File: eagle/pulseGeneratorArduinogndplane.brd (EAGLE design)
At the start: 100 x 80 mm, 64 parts, among them U1 ARDUINOR3-DIMENSION, U2 AD9954YSVZ, U3 LT1962EMS8-1.8PBF, U4 LT1962EMS8-1.8PBF, U7 TXB0108PWR

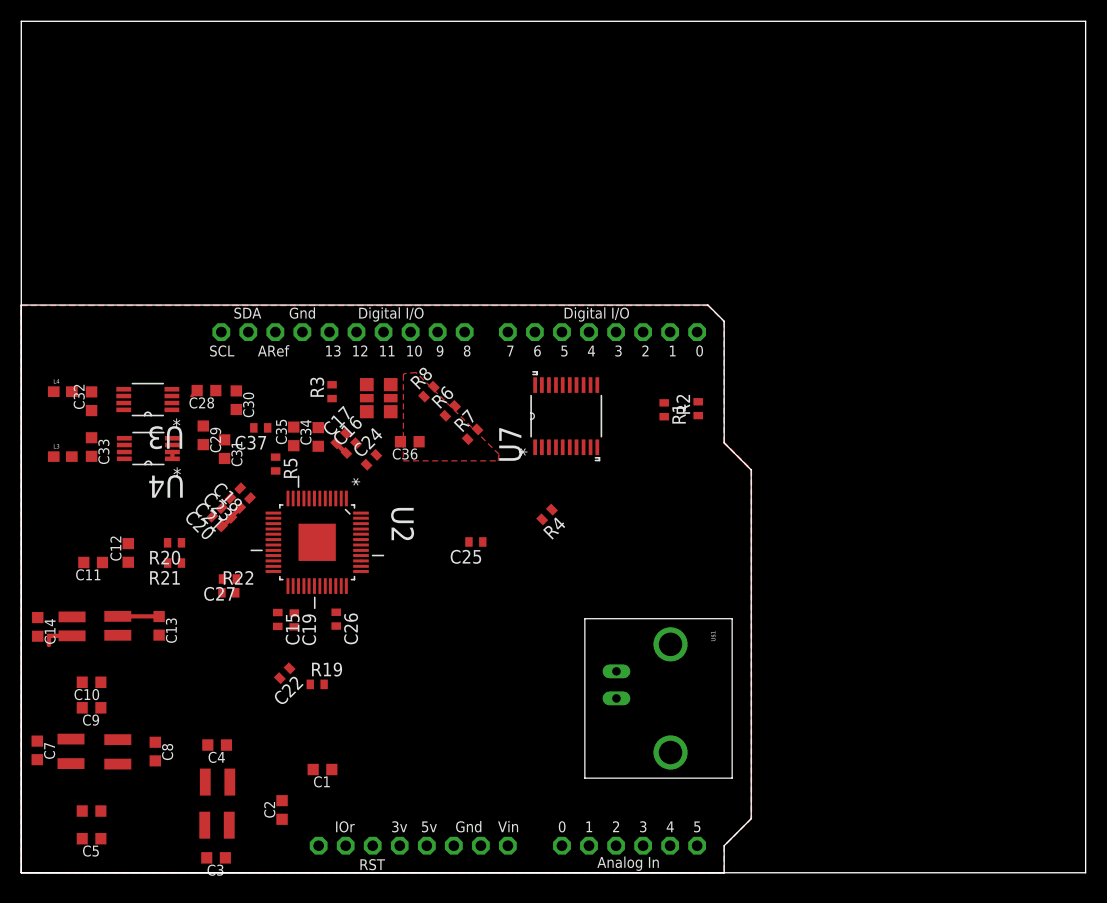
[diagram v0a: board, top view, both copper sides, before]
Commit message: Revert "Deleted all routes to try and fix."
This reverts commit 5f491c1068aea24b9851c2c5770cd8edc15ed6a6.
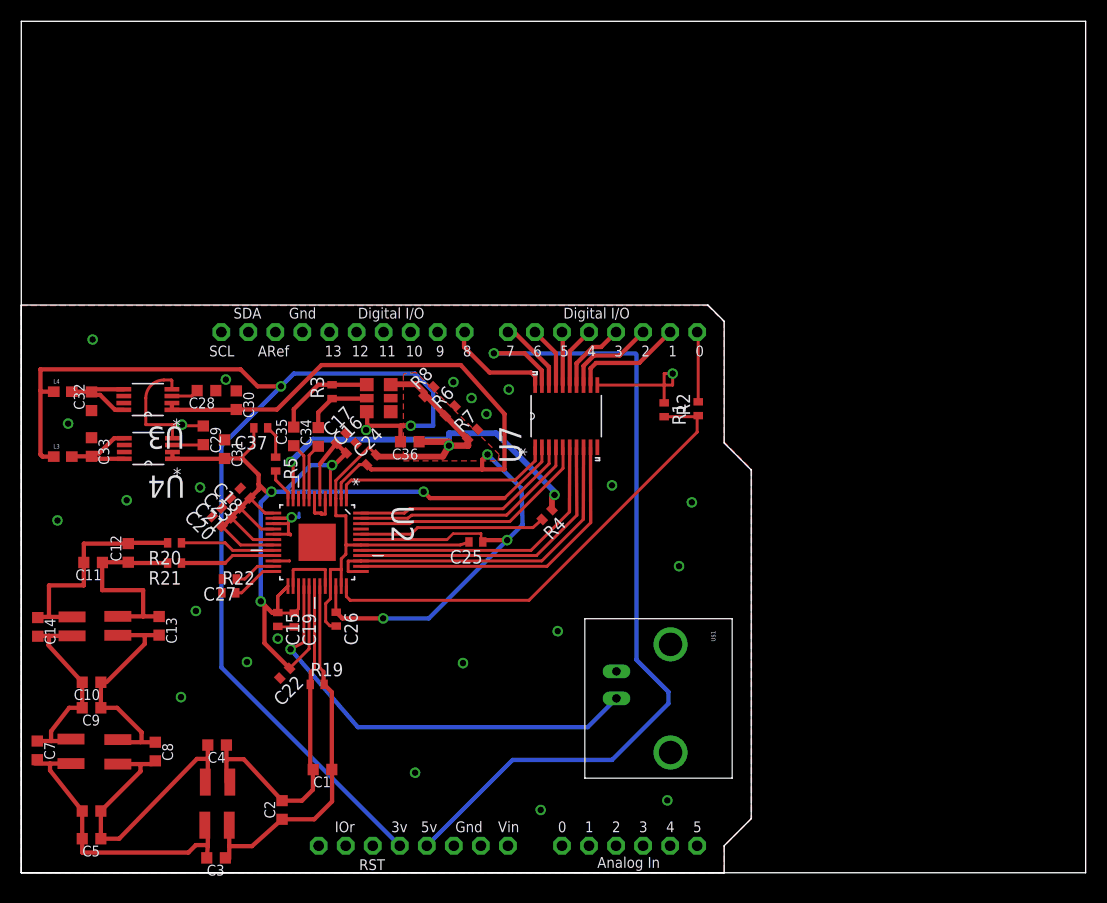
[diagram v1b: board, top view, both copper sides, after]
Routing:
- net +3.3V: track 0.54 -> 132.8 mm, vias 0 -> 2
- net AVDD: track 4.46 -> 121.9 mm, vias 0 -> 4
- net DVDD: track 0.00 -> 106.8 mm, vias 0 -> 3
- net DGND: track 0.00 -> 95.9 mm, vias 0 -> 3
- net +5V: track 0.00 -> 82.3 mm, vias 0 -> 1
- net AGND: track 0.00 -> 47.8 mm, vias 0 -> 26
- net RESET: track 0.00 -> 45.3 mm
- net N$1: track 0.00 -> 41.8 mm, vias 0 -> 1
- net *COMPIN: track 0.00 -> 35.6 mm
- net COMPIN: track 0.39 -> 33.5 mm
- net SS: track 0.01 -> 32.7 mm
- net MISO: track 0.00 -> 30.4 mm
- net N$24: track 0.00 -> 29.2 mm
- net N$20: track 0.00 -> 28.5 mm
- net SCLK: track 0.00 -> 28.2 mm
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- added copper zone on layer 16, net AGND

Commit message: Deleted all routes to try and fix.
This did not stop the crash
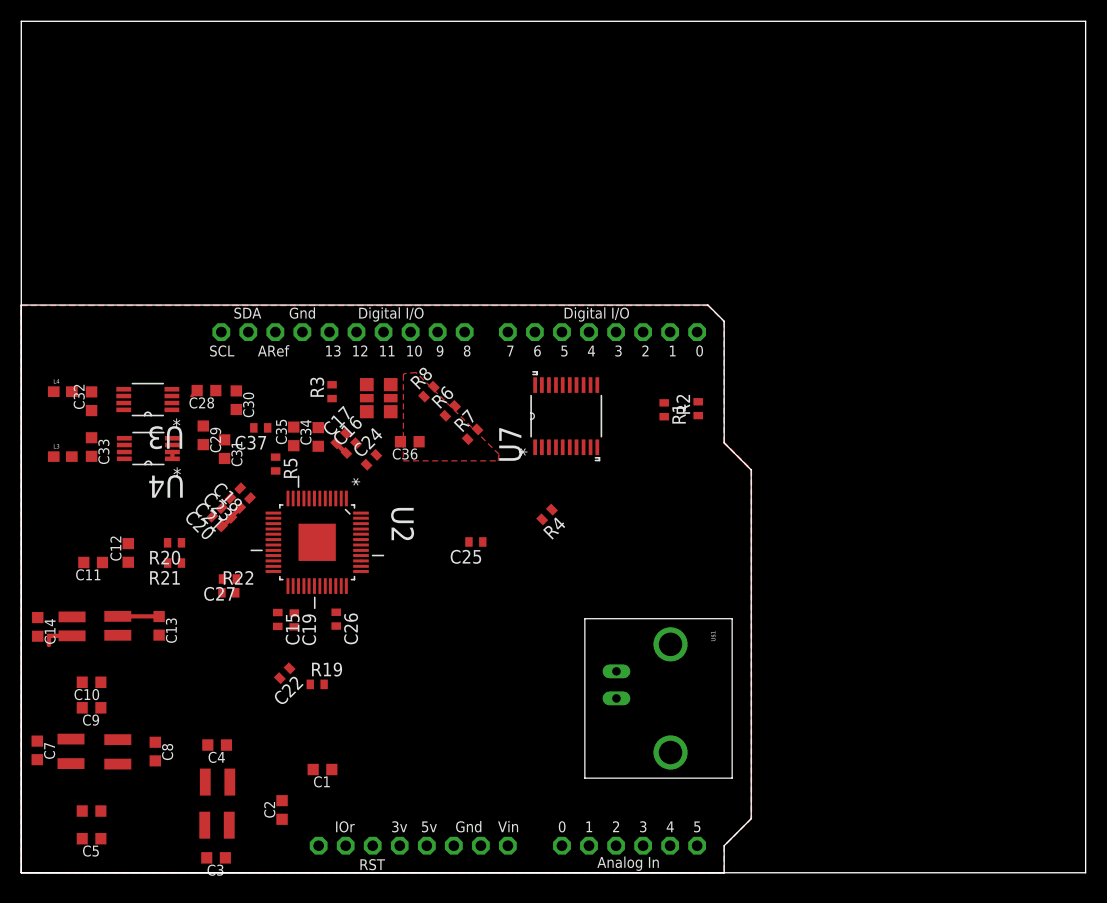
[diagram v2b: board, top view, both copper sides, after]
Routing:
- net +3.3V: track 132.8 -> 0.54 mm, vias 2 -> 0
- net AVDD: track 121.9 -> 4.46 mm, vias 4 -> 0
- net DVDD: track 106.8 -> 0.00 mm, vias 3 -> 0
- net DGND: track 95.9 -> 0.00 mm, vias 3 -> 0
- net +5V: track 82.3 -> 0.00 mm, vias 1 -> 0
- net AGND: track 47.8 -> 0.00 mm, vias 26 -> 0
- net RESET: track 45.3 -> 0.00 mm
- net N$1: track 41.8 -> 0.00 mm, vias 1 -> 0
- net *COMPIN: track 35.6 -> 0.00 mm
- net COMPIN: track 33.5 -> 0.39 mm
- net SS: track 32.7 -> 0.01 mm
- net MISO: track 30.4 -> 0.00 mm
- net N$24: track 29.2 -> 0.00 mm
- net N$20: track 28.5 -> 0.00 mm
- net SCLK: track 28.2 -> 0.00 mm
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- removed copper zone on layer 16, net AGND
